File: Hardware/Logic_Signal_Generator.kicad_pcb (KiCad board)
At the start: 2 copper layers, 70 x 60 mm, 55 parts, among them J1 JTAG, J2 I/O, J3 USB_B, J4 POWER_OUT, Q1 DMG3414U, Q2 DMG3414U, Q3 DMG3414U, Q4 DMG3414U, Q5 DMG3414U, Q6 DMG3414U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

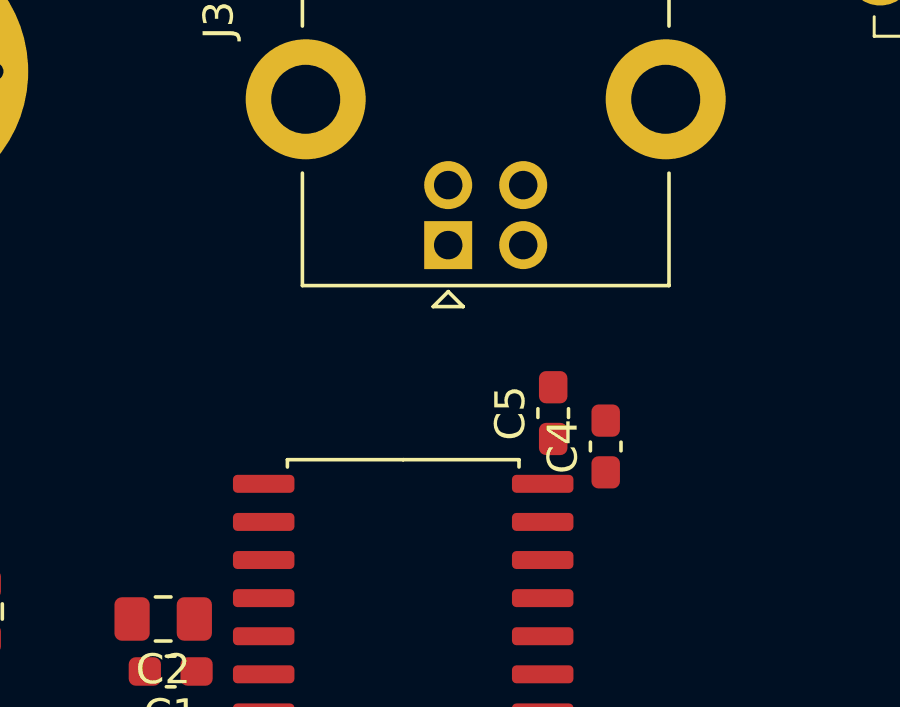
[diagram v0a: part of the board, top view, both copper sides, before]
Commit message: [Hardware] Routed the USB full speed traces trying to keep a matched length and a 45ohm odd differential impedance.
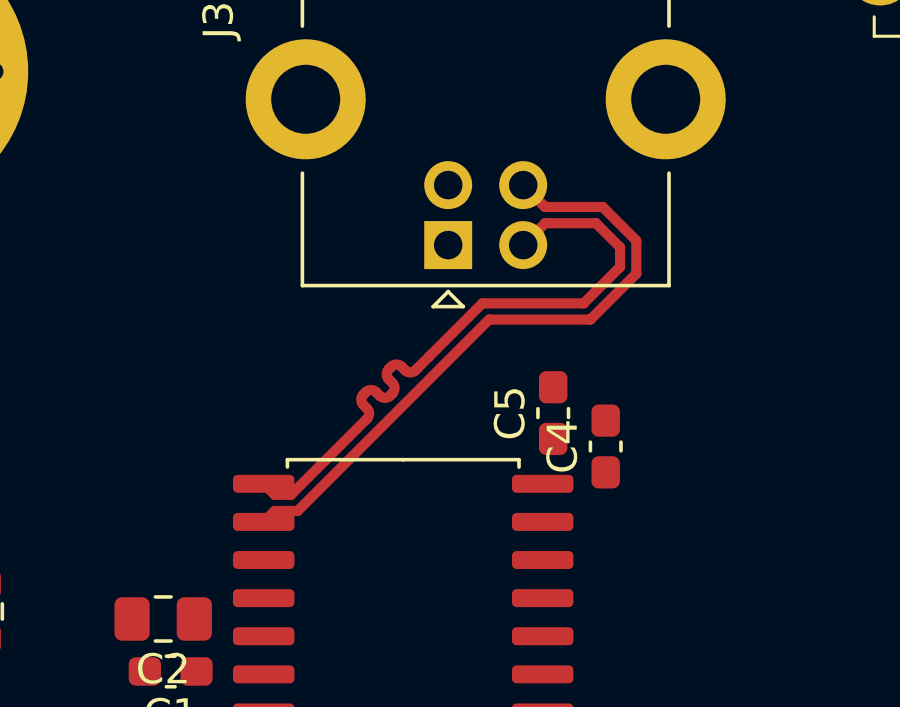
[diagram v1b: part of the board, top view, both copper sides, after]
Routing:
- net /USB_D+: track 0.00 -> 21.5 mm
- net /USB_D-: track 0.00 -> 21.4 mm

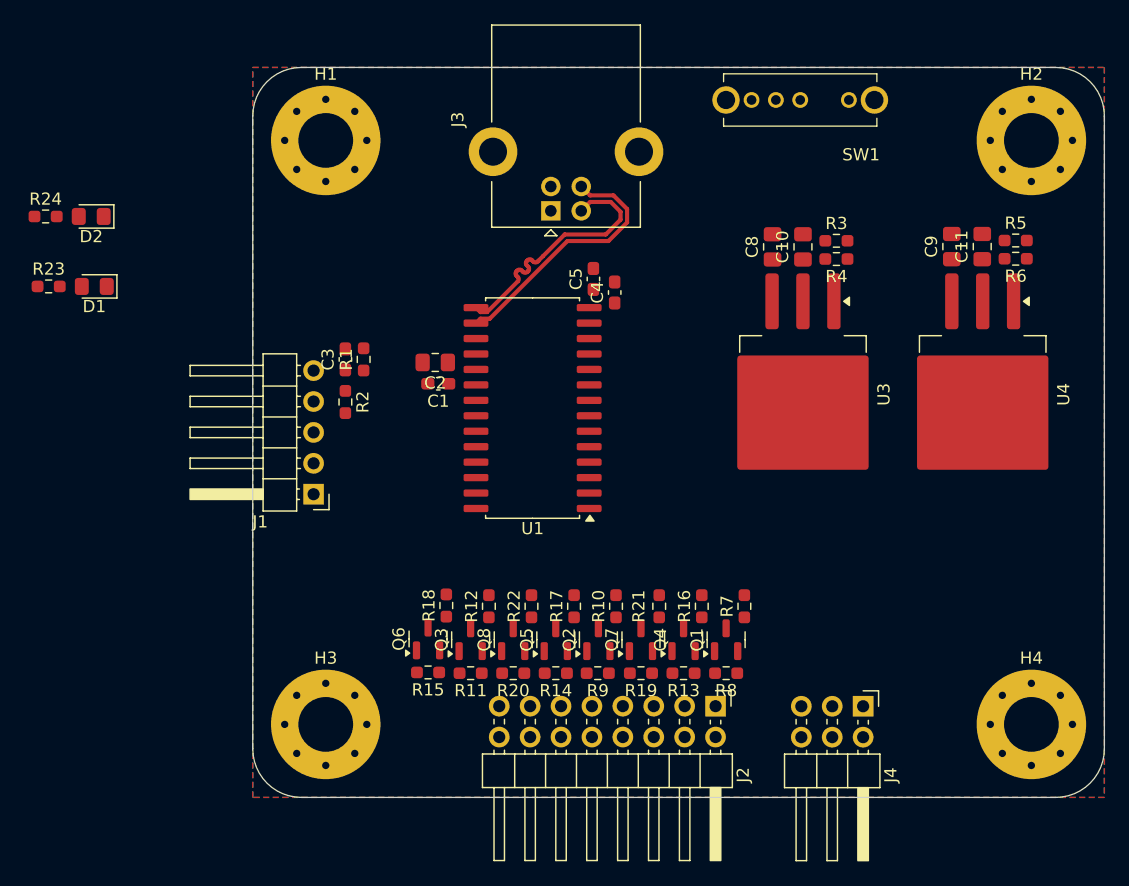
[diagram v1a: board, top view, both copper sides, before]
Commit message: [Hardware] Routed the voltage regulators.
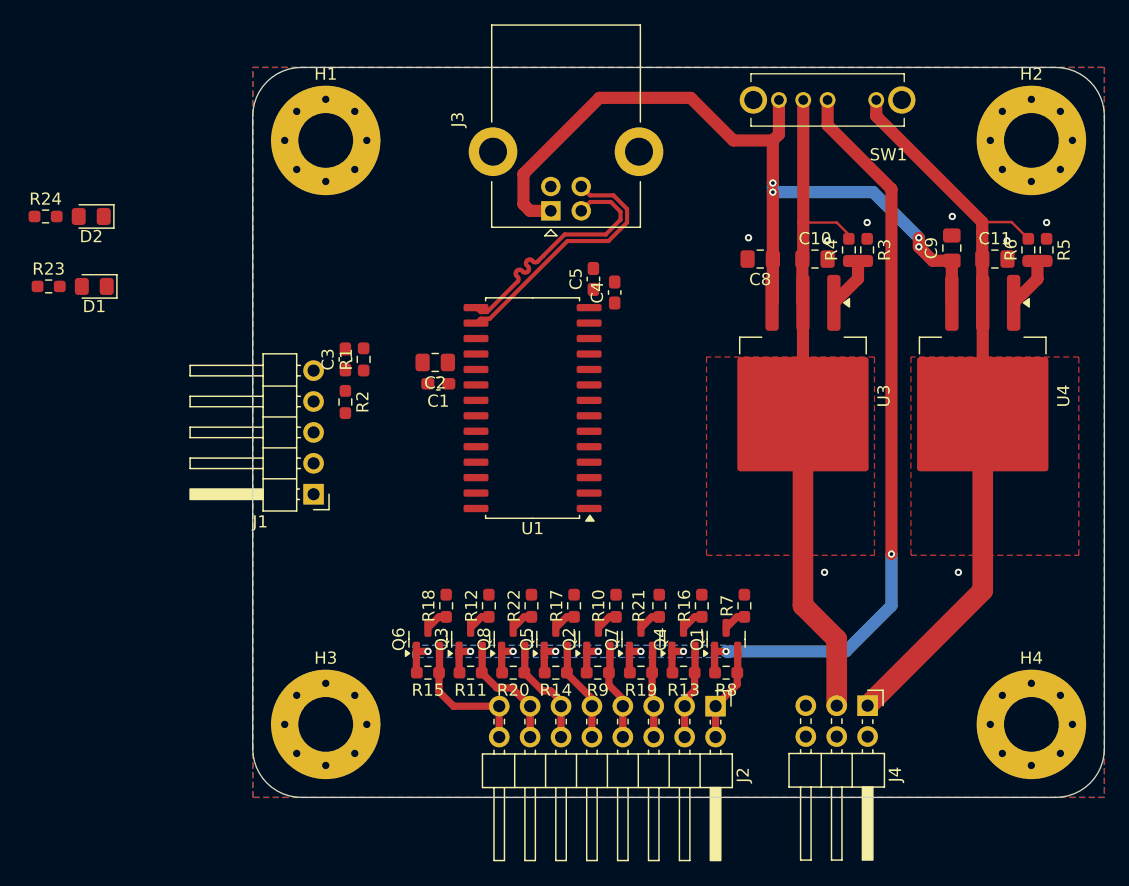
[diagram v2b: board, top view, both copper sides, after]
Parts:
- moved R5 2.66 mm to (193.2, 94.0), turned to -90 degrees
- moved R3 2.63 mm to (178.5, 94.0), turned to -90 degrees
- moved SW1 2.25 mm to (175.2, 81.7)
- moved C11 1.46 mm to (189.0, 94.8), turned to 0 degrees
- moved C8 1.42 mm to (169.7, 94.8), turned to 180 degrees
- moved C10 1.41 mm to (174.2, 94.8), turned to 0 degrees
- moved R4 1.27 mm to (177.0, 94.0), turned to 90 degrees
- moved R6 1.27 mm to (191.8, 94.0), turned to 90 degrees
- moved J4 0.37 mm to (178.5, 131.5)
- moved C9 0.12 mm to (185.5, 93.8)
- moved U3 0.12 mm to (173.2, 106.0)
- moved U4 0.12 mm to (188.0, 106.0)
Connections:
- J4 pad 1: +5V -> +1V8
- J4 pad 5: +1V8 -> +5V
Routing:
- net VCC: track 0.00 -> 81.3 mm, vias 0 -> 9
- net +5V: track 0.00 -> 67.4 mm, vias 0 -> 4
- net +1V8: track 0.00 -> 61.7 mm
- net +3.3V: track 0.00 -> 55.5 mm
- net /Voltage_Shifter/IO8: track 0.00 -> 11.4 mm
- net /Voltage_Shifter/IO7: track 0.00 -> 9.48 mm
- net /Voltage_Shifter/IO6: track 0.00 -> 8.76 mm
- net /Voltage_Shifter/IO5: track 0.00 -> 7.97 mm
- net /Voltage_Shifter/IO1: track 0.00 -> 7.86 mm
- net /Voltage_Shifter/IO4: track 0.00 -> 7.61 mm
- net /Voltage_Shifter/IO2: track 0.00 -> 7.46 mm
- net /Voltage_Shifter/IO3: track 0.00 -> 7.17 mm
- net Net-(U3-ADJ): track 0.00 -> 5.76 mm
- net Net-(U4-ADJ): track 0.00 -> 5.75 mm
- net /TX: track 0.00 -> 1.87 mm
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- added copper zone on F.Cu, net +1V8
- added copper zone on F.Cu, net +3.3V
- added copper zone on B.Cu, net VCC

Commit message: [Hardware] Routed all but the LEDs.
Changed the IOs order to help the routing.
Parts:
- moved R2 0.88 mm to (136.5, 106.5), turned to 180 degrees
- moved C4 0.10 mm to (157.8, 97.6)
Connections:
- Q1 pad 3: /SDA -> /P1A
- Q2 pad 3: /SCL -> /SDA
- Q4 pad 3: /P1B -> /TX
- Q5 pad 3: /RX -> /SCL
- Q6 pad 3: /TX -> /P1D
- Q7 pad 3: /P1D -> /RX
- Q8 pad 3: /P1A -> /P1B
- R10 pad 1: /SCL -> /SDA
- R16 pad 1: /P1B -> /TX
- R17 pad 1: /RX -> /SCL
- R18 pad 1: /TX -> /P1D
- R21 pad 1: /P1D -> /RX
- R22 pad 1: /P1A -> /P1B
- R7 pad 1: /SDA -> /P1A
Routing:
- net +5V: track 67.4 -> 167.0 mm, vias 4 -> 11
- net /TX: track 1.87 -> 36.6 mm
- net /RX: track 1.87 -> 33.6 mm
- net /P1A: track 1.87 -> 33.0 mm
- net /~{MCLR}: track 0.00 -> 30.4 mm, vias 0 -> 2
- net /SDA: track 1.87 -> 30.4 mm
- net /SCL: track 1.82 -> 26.3 mm
- net Net-(J1-Pin_2): track 0.00 -> 22.2 mm
- net /P1B: track 1.87 -> 22.2 mm
- net /MOSI: track 1.87 -> 18.9 mm
- net /P1D: track 1.87 -> 18.0 mm
- net Net-(J1-Pin_1): track 0.00 -> 13.4 mm
- net Net-(J1-Pin_5): track 0.00 -> 6.87 mm
- net VCC: track 81.3 -> 82.9 mm
- net GND: vias 8 -> 17
- added copper zone on B.Cu, net +5V
- added copper zone on F.Cu, net Net-(U1-VUSB3V3/VDDCORE)

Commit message: [Hardware] Routed the LEDs and changed their current limiting resistors package.
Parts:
- R23, R24: footprint Resistor_SMD:R_0603_1608Metric_Pad0.98x0.95mm_HandSolder -> Resistor_SMD:R_1206_3216Metric_Pad1.30x1.75mm_HandSolder
- moved R24 23.1 mm to (134.0, 92.8), turned to 180 degrees
- moved R23 22.8 mm to (134.0, 97.5), turned to 180 degrees
- moved D2 15.9 mm to (130.5, 92.8), turned to 90 degrees
- moved D1 15.5 mm to (130.5, 97.5), turned to 90 degrees
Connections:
- U1 pad 11: /LED_USB -> /LED_POWER
- U1 pad 12: /LED_POWER -> /LED_USB
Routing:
- net /LED_USB: track 0.00 -> 23.6 mm, vias 0 -> 2
- net /LED_POWER: track 0.00 -> 22.2 mm, vias 0 -> 2
- net Net-(D1-A): track 0.00 -> 2.37 mm
- net Net-(D2-A): track 0.00 -> 2.35 mm
- net GND: vias 17 -> 21

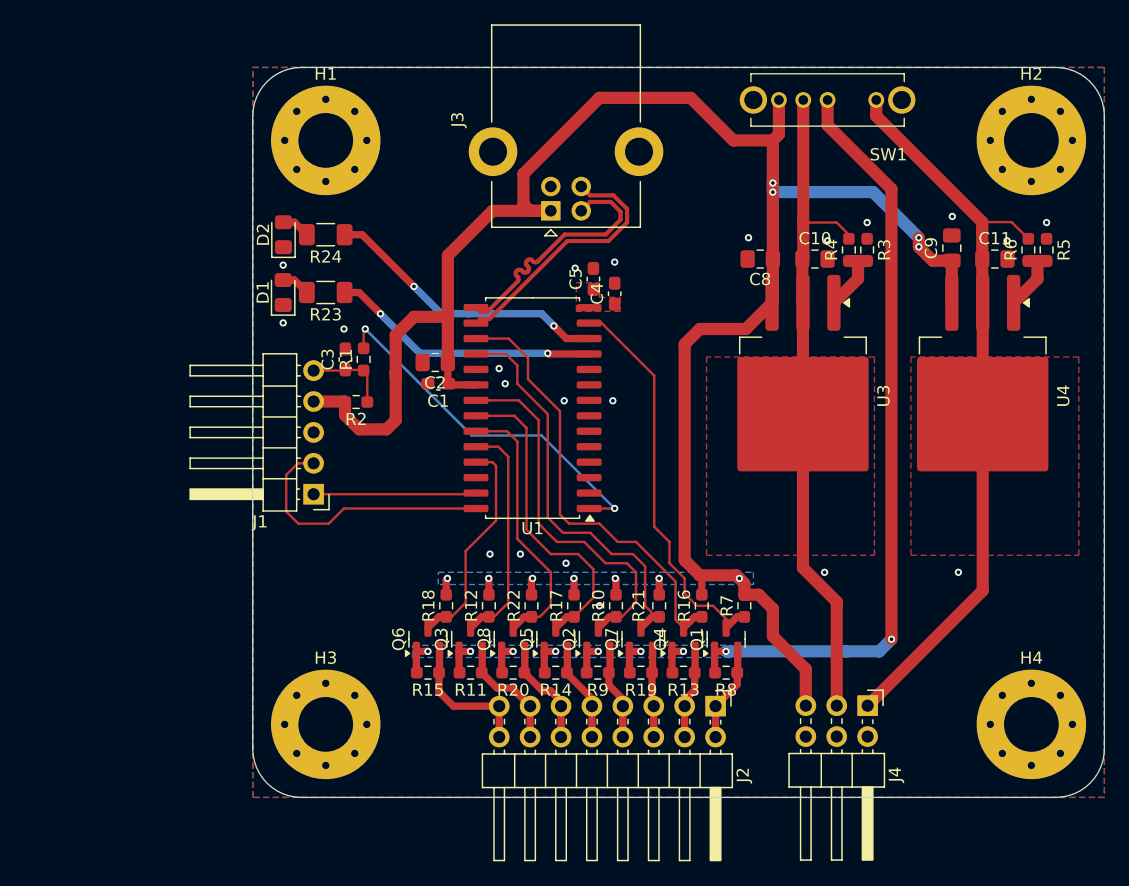
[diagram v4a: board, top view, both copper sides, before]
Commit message: [Hardware] Added the LDO thermal pads and the connectors and LEDs silkscreen marking.
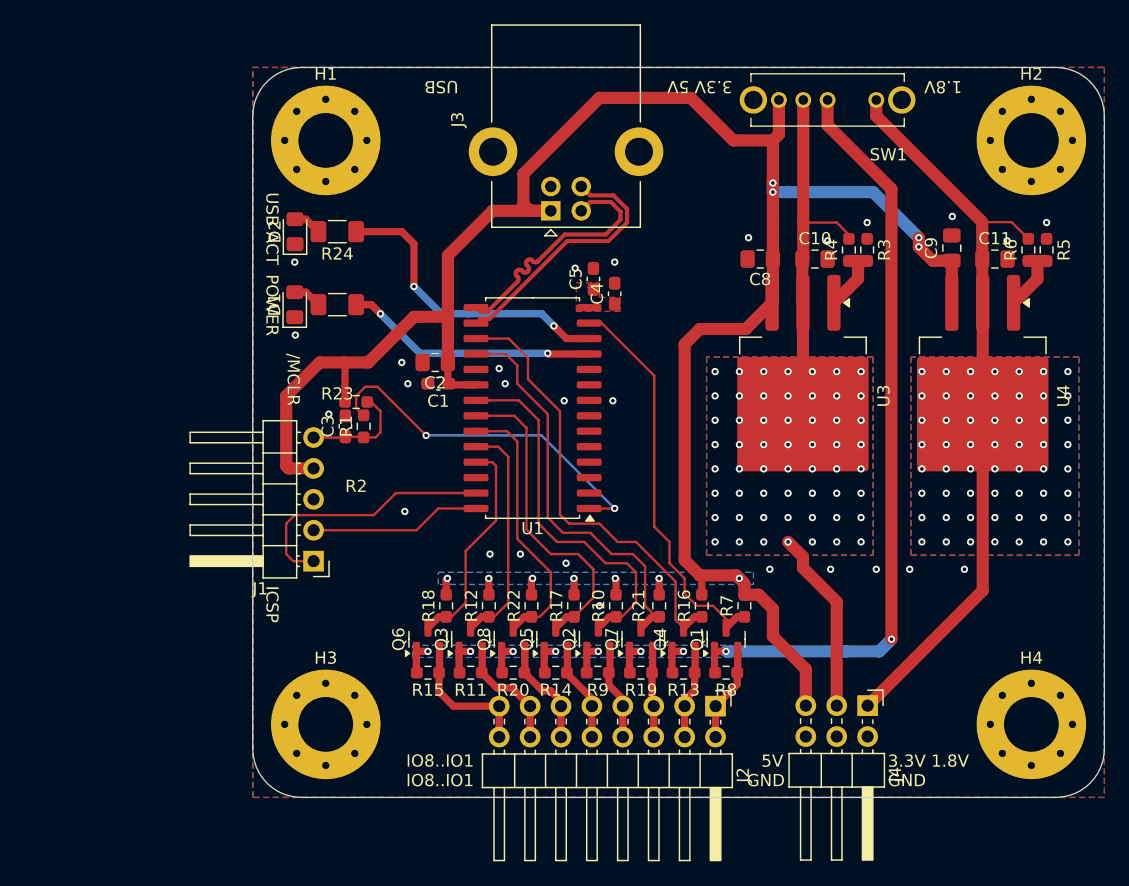
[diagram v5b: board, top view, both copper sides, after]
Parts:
- moved C3 5.50 mm to (135.6, 108.5)
- moved J1 5.50 mm to (133.0, 119.6)
- moved R1 5.50 mm to (137.1, 108.5)
- moved D1 1.38 mm to (131.4, 98.5)
- moved R23 1.38 mm to (134.9, 98.5)
- moved D2 0.98 mm to (131.5, 92.5)
- moved R24 0.98 mm to (134.9, 92.5)
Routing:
- net +3.3V: track 55.5 -> 45.5 mm, vias 0 -> 56
- net Net-(J1-Pin_1): track 13.4 -> 21.6 mm
- net Net-(J1-Pin_2): track 22.2 -> 14.1 mm
- net +5V: track 167.0 -> 173.3 mm
- net Net-(J1-Pin_5): track 6.87 -> 8.86 mm
- net /LED_POWER: track 22.2 -> 20.8 mm
- net /LED_USB: track 23.6 -> 24.8 mm
- net /~{MCLR}: track 30.4 -> 29.6 mm
- net GND: vias 21 -> 27
- net +1V8: vias 0 -> 56
- added copper zone on B.Cu, net +1V8
- added copper zone on B.Cu, net +3.3V
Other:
- board text added: "/MCLR"
- board text added: "1.8V"
- board text added: "3.3V 1.8V"
- board text added: "3.3V 5V"
- board text added: "5V"
- board text added: "GND"
- board text added: "ICSP"
- board text added: "IO8..IO1 IO8..IO1"
- board text added: "POWER"
- board text added: "USB"
- board text added: "USB ACT"

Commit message: [Hardware] Fixed all remaining silkscreen-related PCB warnings.
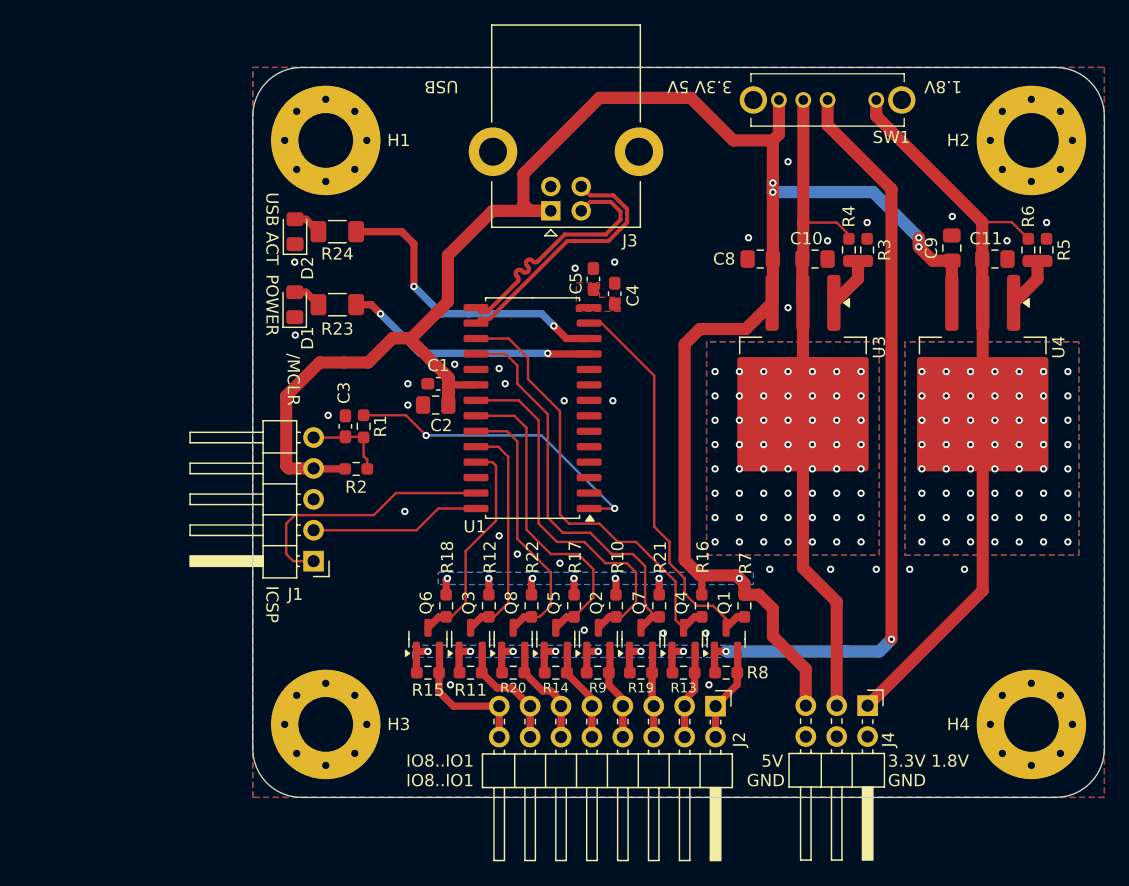
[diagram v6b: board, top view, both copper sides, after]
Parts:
- moved R2 5.50 mm to (136.5, 112.0)
- moved C2 3.50 mm to (143.0, 106.8)
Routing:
- net +3.3V: track 45.5 -> 56.4 mm
- net +5V: track 173.3 -> 177.8 mm
- net /~{MCLR}: track 29.6 -> 25.9 mm
- net Net-(J1-Pin_5): track 8.86 -> 6.87 mm
- net GND: vias 27 -> 34

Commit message: [Hardware] Added the USB connector 3D model to the PCB.
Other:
- board text added: "13/09/2025"
